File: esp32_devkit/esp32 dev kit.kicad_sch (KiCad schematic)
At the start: 21 parts, among them J1 Conn_01x03_Pin, J2 Conn_01x03_Pin, J3 Conn_01x15_Pin, J4 Conn_01x15_Pin, P1 USB_C_Plug, Q1 NPN, Q2 NPN, U1 ESP32-WROOM-32, U2 CH340C, U3 AMS1117-3.3

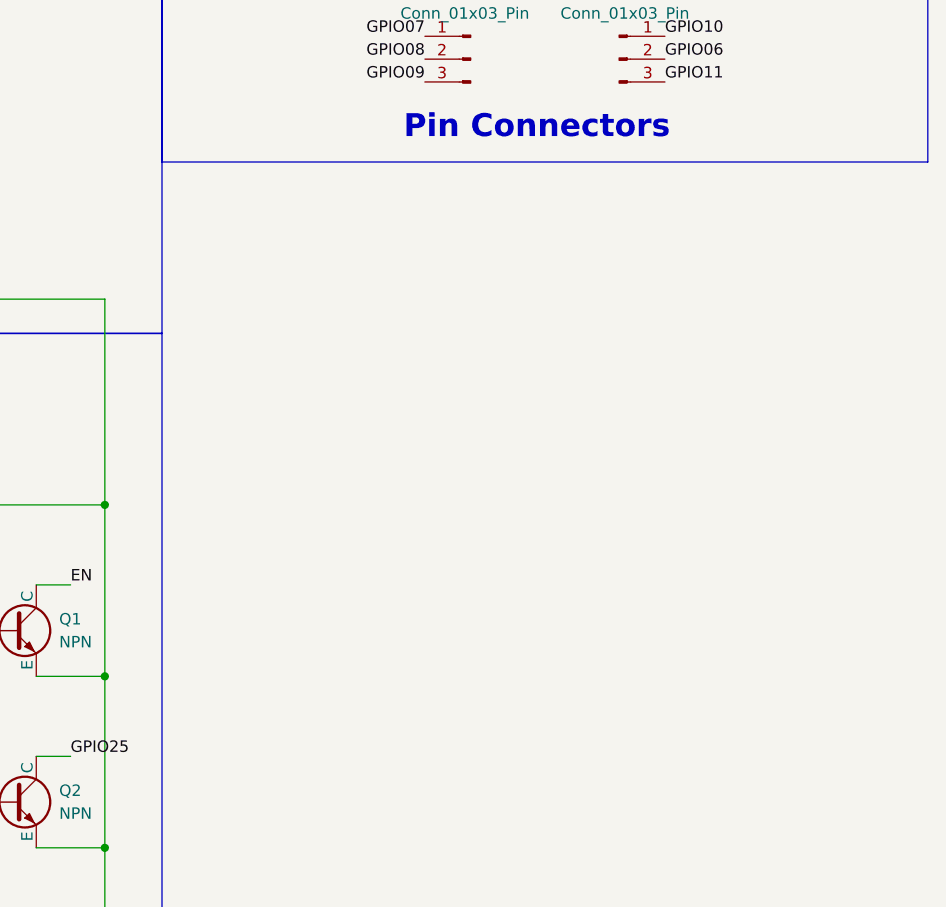
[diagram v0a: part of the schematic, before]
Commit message: added smarthome
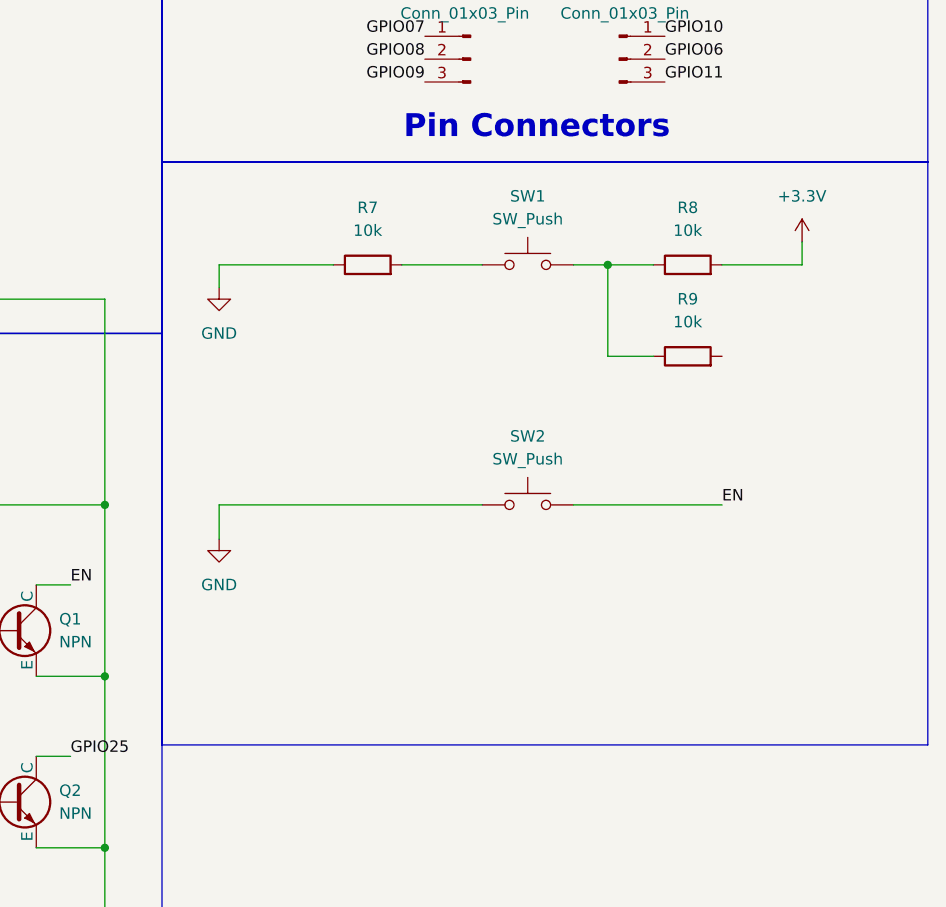
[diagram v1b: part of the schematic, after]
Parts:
- added R7, R8, R9: 10k, Resistor_THT:R_Axial_DIN0207_L6.3mm_D2.5mm_P7.62mm_Horizontal, symbol Device:R
- added SW1, SW2: SW_Push, symbol Switch:SW_Push
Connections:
- net EN: now also SW2.2
- net GND: now also R7.1, SW2.1
- new net: R8.1, R9.1, SW1.2
- new net: R7.2, SW1.1
- new net +3.3V: R8.2
